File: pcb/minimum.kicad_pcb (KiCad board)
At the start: 4 copper layers, 16 x 20 mm, 31 parts, among them J1 USB4155-03-C_REVA, U1 RP2040, U2 SCD4x, U3 W25Q16JVUXIQ_WIN, U4 XCL220, Y1 C2E-12.000-18-1020-X-R

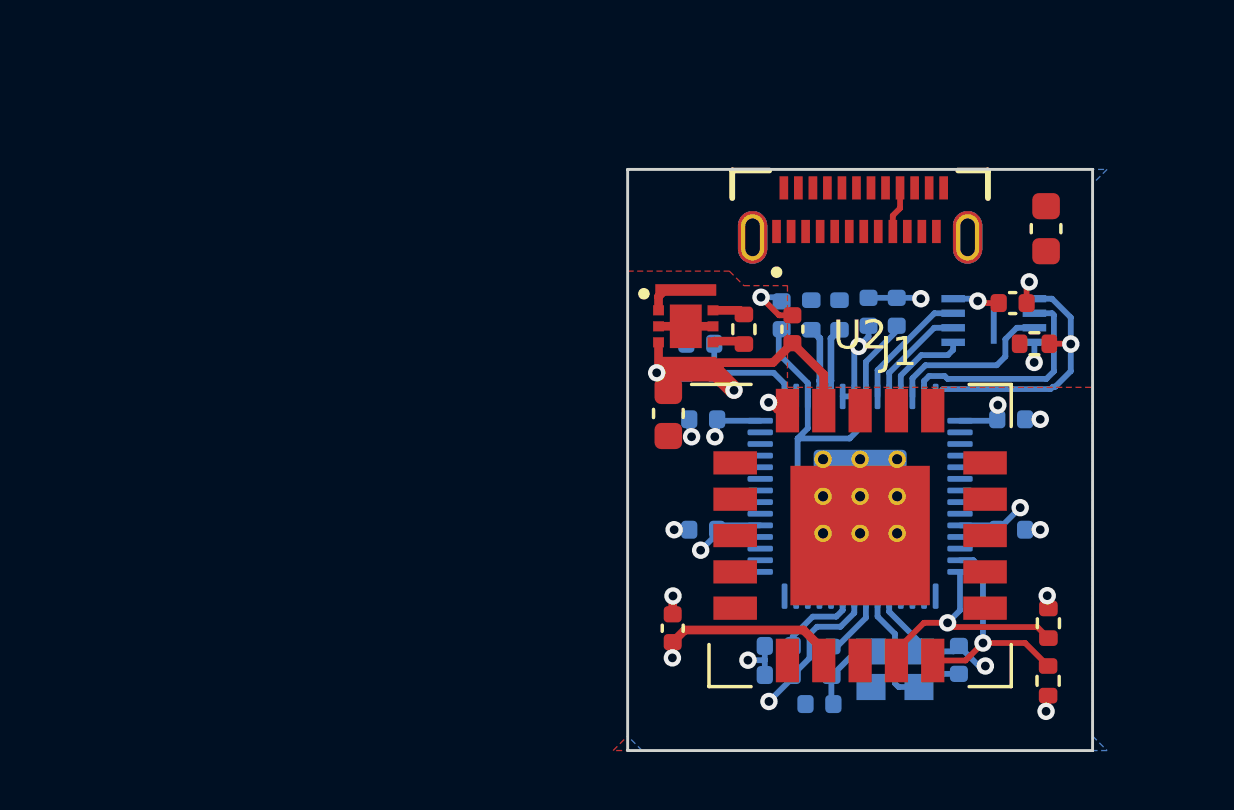
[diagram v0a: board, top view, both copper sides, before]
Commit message: USB plug connector changed to DX07P024MJ1R1500
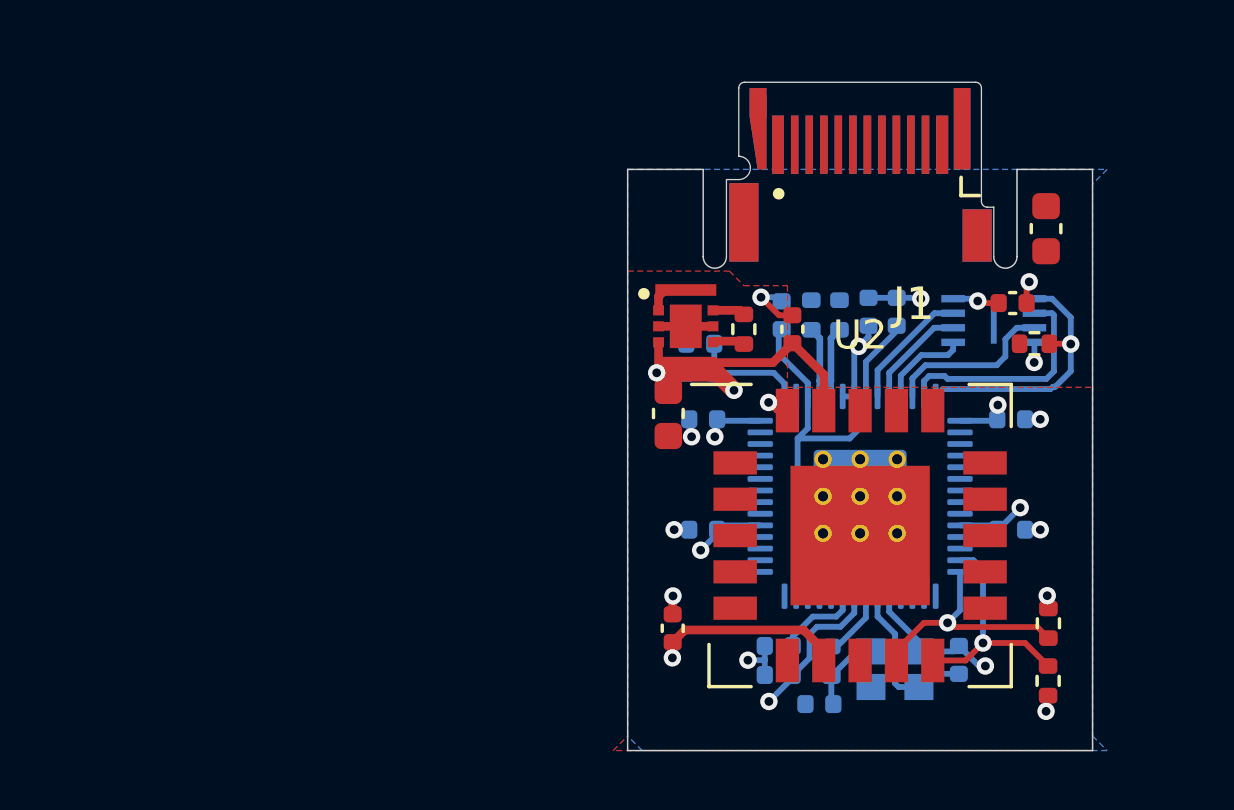
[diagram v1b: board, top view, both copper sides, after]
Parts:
- J1: value USB4155-03-C_REVA -> DX07P024MJ1R1500; footprint SMD:GCT_USB4155-03-C_REVA -> SMD:JAE_DX07P024MJ1R1500
- U3: value W25Q16JVUXIQ_WIN -> W25Q16JVUXIQ
- moved J1 4.39 mm to (100.0, 57.0)
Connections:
- J1 pad A10: (no net) -> unconnected-(J1-PadA10)
- J1 pad A11: (no net) -> unconnected-(J1-PadA11)
- J1 pad A2: (no net) -> unconnected-(J1-PadA2)
- J1 pad A3: (no net) -> unconnected-(J1-PadA3)
- J1 pad A4: VBUS -> Net-(J1-PadA4)
- J1 pad A5: (no net) -> unconnected-(J1-PadA5)
- J1 pad A6: /USB_D+ -> unconnected-(J1-PadA6)
- J1 pad A7: /USB_D- -> unconnected-(J1-PadA7)
- J1 pad A8: (no net) -> unconnected-(J1-PadA8)
- J1 pad A9: VBUS -> Net-(J1-PadA4)
- J1 pad B10: (no net) -> unconnected-(J1-PadB10)
- J1 pad B11: (no net) -> unconnected-(J1-PadB11)
- J1 pad B2: (no net) -> unconnected-(J1-PadB2)
- J1 pad B3: (no net) -> unconnected-(J1-PadB3)
- J1 pad B4: VBUS -> Net-(J1-PadB4)
- J1 pad B5: (no net) -> unconnected-(J1-PadB5)
- J1 pad B6: /USB_D+ -> unconnected-(J1-PadB6)
- J1 pad B7: /USB_D- -> unconnected-(J1-PadB7)
- J1 pad B8: (no net) -> unconnected-(J1-PadB8)
- J1 pad B9: VBUS -> Net-(J1-PadB4)
- J1 pad S1: Net-(J1-PadS1) -> (no net)
- J1 pad S2: Net-(J1-PadS1) -> (no net)
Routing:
- net VBUS: track 1.60 -> 0.00 mm
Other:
- outline, holes or cut-outs redrawn

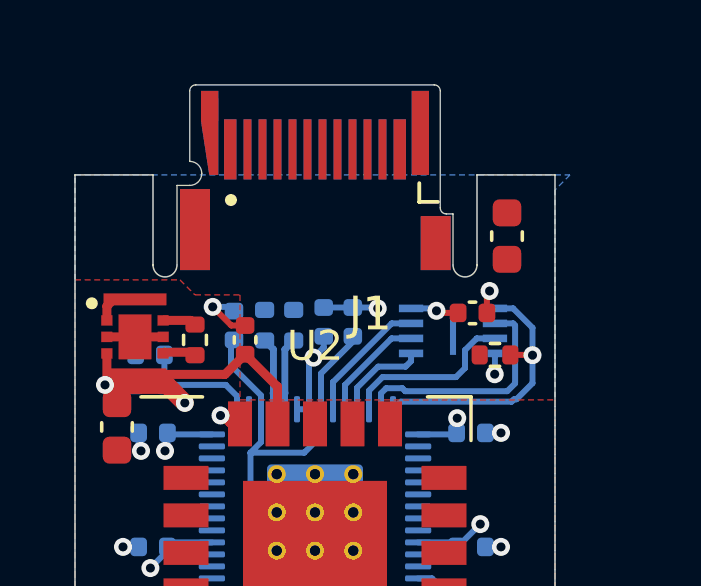
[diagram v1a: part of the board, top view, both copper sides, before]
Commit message: routing VBUS
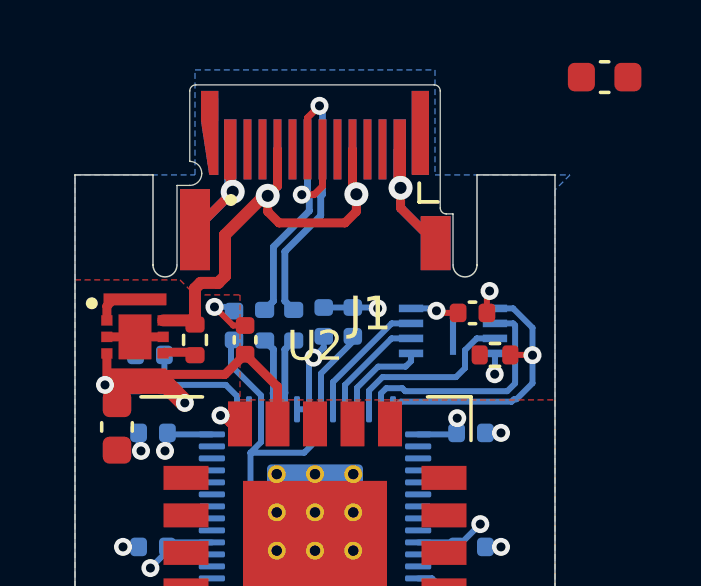
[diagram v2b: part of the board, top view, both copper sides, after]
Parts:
- moved C17 6.22 mm to (109.7, 56.7), turned to 180 degrees
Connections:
- J1 pad A1: Net-(J1-PadA1) -> GND
- J1 pad A10: unconnected-(J1-PadA10) -> (no net)
- J1 pad A11: unconnected-(J1-PadA11) -> (no net)
- J1 pad A12: Net-(J1-PadA1) -> GND
- J1 pad A2: unconnected-(J1-PadA2) -> (no net)
- J1 pad A3: unconnected-(J1-PadA3) -> (no net)
- J1 pad A4: Net-(J1-PadA4) -> VBUS
- J1 pad A5: unconnected-(J1-PadA5) -> (no net)
- J1 pad A6: unconnected-(J1-PadA6) -> /USB_D+
- J1 pad A7: unconnected-(J1-PadA7) -> /USB_D-
- J1 pad A8: unconnected-(J1-PadA8) -> (no net)
- J1 pad A9: Net-(J1-PadA4) -> VBUS
- J1 pad B1: Net-(J1-PadB1) -> GND
- J1 pad B10: unconnected-(J1-PadB10) -> (no net)
- J1 pad B11: unconnected-(J1-PadB11) -> (no net)
- J1 pad B12: Net-(J1-PadB1) -> GND
- J1 pad B2: unconnected-(J1-PadB2) -> (no net)
- J1 pad B3: unconnected-(J1-PadB3) -> (no net)
- J1 pad B4: Net-(J1-PadB4) -> VBUS
- J1 pad B5: unconnected-(J1-PadB5) -> (no net)
- J1 pad B6: unconnected-(J1-PadB6) -> /USB_D+
- J1 pad B7: unconnected-(J1-PadB7) -> /USB_D-
- J1 pad B8: unconnected-(J1-PadB8) -> (no net)
- J1 pad B9: Net-(J1-PadB4) -> VBUS
- J1 pad S3: Net-(J1-PadS3) -> GND
- J1 pad S4: Net-(J1-PadS3) -> GND
- J1 pad S5: Net-(J1-PadS3) -> GND
- J1 pad S6: Net-(J1-PadS3) -> GND
- R7 pad 1: +5V -> VBUS
- U4 pad 6: +5V -> VBUS
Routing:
- net VBUS: track 0.00 -> 17.7 mm, vias 0 -> 2
- net GND: track 19.4 -> 33.0 mm, vias 12 -> 14
- net /USB_D-: track 0.00 -> 9.62 mm, vias 0 -> 1
- net /USB_D+: track 0.00 -> 9.10 mm, vias 0 -> 1
- net +5V: track 1.12 -> 0.00 mm
- net +3V3: track 42.4 -> 43.4 mm

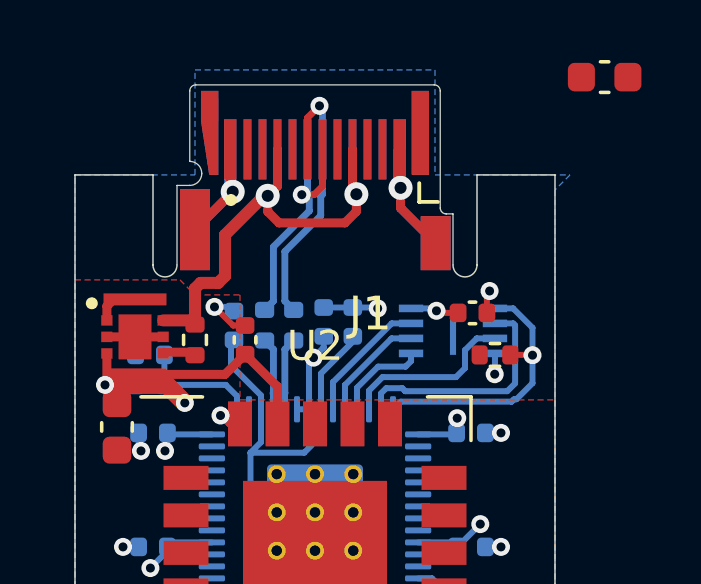
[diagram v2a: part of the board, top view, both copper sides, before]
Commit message: routing VBUS
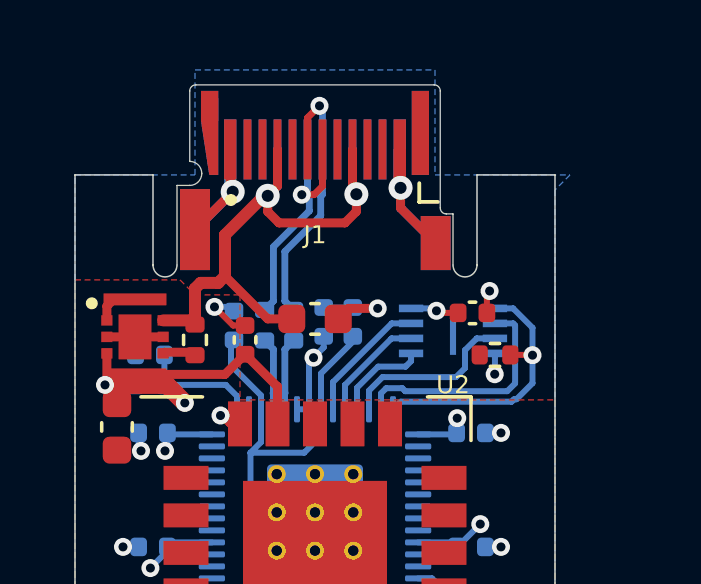
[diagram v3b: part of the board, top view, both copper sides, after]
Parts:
- moved C17 12.6 mm to (100.0, 64.8), turned to 0 degrees
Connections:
- C17 pad 1: (no net) -> VBUS
- C17 pad 2: (no net) -> GND
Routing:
- net VBUS: track 17.7 -> 20.5 mm
- net GND: track 33.0 -> 34.4 mm
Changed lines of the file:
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@@
     (property "Sheetname" "")
     (attr through_hole)
-    (fp_text reference "U2" (at 0 -6.9) (layer "F.SilkS")
-      (effects (font (size 1 1) (thickness 0.15)))
+    (fp_text reference "U2" (at 4.6 -5.6) (layer "F.SilkS")
+      (effects (font (size 0.6 0.6) (thickness 0.15)))
     )
     (fp_text value "SCD4x" (at 0 6.9) (layer "F.Fab")
@@
   )
   (footprint "Capacitor_SMD:C_0603_1608Metric" (layer "F.Cu")
-    (at 109.655 56.74 180)
+    (at 100 64.8)
     (descr "Capacitor SMD 0603 (1608 Metric), square (rectangular) end terminal, IPC_7351 nominal, (Body size source: IPC-SM-782 page 76, https://www.pcb-3d.com/wordpress/wp-content/uploads/ipc-sm-782a_amendment_1_and_2.pdf), generated with kicad-footprint-generator")
     (tags "capacitor")
@@
     (fp_line (start -0.8 0.4) (end -0.8 -0.4) (layer "F.Fab") (width 0.1))
     (fp_line (start 0.8 -0.4) (end 0.8 0.4) (layer "F.Fab") (width 0.1))
-    (pad "1" smd roundrect locked (at -0.775 0 180) (size 0.9 0.95) (layers "F.Cu" "F.Paste" "F.Mask") (roundrect_rratio 0.25)
-      (pintype "passive"))
-    (pad "2" smd roundrect locked (at 0.775 0 180) (size 0.9 0.95) (layers "F.Cu" "F.Paste" "F.Mask") (roundrect_rratio 0.25)
-      (pintype "passive"))
+    (pad "1" smd roundrect locked (at -0.775 0) (size 0.9 0.95) (layers "F.Cu" "F.Paste" "F.Mask") (roundrect_rratio 0.25)
+      (net 21 "VBUS") (pintype "passive"))
+    (pad "2" smd roundrect locked (at 0.775 0) (size 0.9 0.95) (layers "F.Cu" "F.Paste" "F.Mask") (roundrect_rratio 0.25)
+      (net 3 "GND") (pintype "passive"))
     (model "${KISYS3DMOD}/Capacitor_SMD.3dshapes/C_0603_1608Metric.wrl"
       (offset (xyz 0 0 0))
@@
     (property "Sheetname" "")
     (attr through_hole)
-    (fp_text reference "J1" (at -1.83903 -7.62843 180) (layer "F.SilkS")
-      (effects (font (size 1.125087 1.125087) (thickness 0.15)))
+    (fp_text reference "J1" (at 0 -5 180) (layer "F.SilkS")
+      (effects (font (size 0.6 0.6) (thickness 0.15)))
     )
     (fp_text value "DX07P024MJ1R1500" (at 9.24037 2.245715 180) (layer "F.Fab")
@@
   (segment (start 105.73 64.6) (end 105.73 63.96) (width 0.2) (layer "F.Cu") (net 3))
   (segment (start 97.2695 65.02) (end 96.6495 64.4) (width 0.2) (layer "F.Cu") (net 3))
+  (segment (start 101.125 64.45) (end 100.775 64.8) (width 0.3) (layer "F.Cu") (net 3))
   (segment (start 97.67 65.02) (end 97.2695 65.02) (width 0.2) (layer "F.Cu") (net 3))
   (segment (start 97.175 59.15) (end 97.175 60.480534) (width 0.3) (layer "F.Cu") (net 3))
@@
   (segment (start 105.73 63.96) (end 105.82 63.87) (width 0.2) (layer "F.Cu") (net 3))
   (segment (start 94.375 65.4) (end 94 65.025) (width 0.3) (layer "F.Cu") (net 3))
+  (segment (start 102.09 64.45) (end 101.125 64.45) (width 0.3) (layer "F.Cu") (net 3))
   (segment (start 102.825 60.403878) (end 102.852183 60.431061) (width 0.4) (layer "F.Cu") (net 3))
   (segment (start 102.852183 61.102183) (end 104.025 62.275) (width 0.3) (layer "F.Cu") (net 3))
@@
   (segment (start 101.378654 61.221346) (end 101 61.6) (width 0.3) (layer "F.Cu") (net 21))
   (segment (start 97 62) (end 97 63.374022) (width 0.4) (layer "F.Cu") (net 21))
+  (segment (start 98.425978 64.8) (end 97 63.374022) (width 0.3) (layer "F.Cu") (net 21))
   (segment (start 96 63.7875) (end 96 64.99) (width 0.4) (layer "F.Cu") (net 21))
   (segment (start 98.42382 61.22382) (end 98.8 61.6) (width 0.3) (layer "F.Cu") (net 21))
@@
   (segment (start 97 63.374022) (end 96.774022 63.6) (width 0.4) (layer "F.Cu") (net 21))
   (segment (start 98.302248 60.697752) (end 97 62) (width 0.4) (layer "F.Cu") (net 21))
+  (segment (start 99.225 64.8) (end 98.425978 64.8) (width 0.3) (layer "F.Cu") (net 21))
   (segment (start 96.1875 63.6) (end 96 63.7875) (width 0.4) (layer "F.Cu") (net 21))
   (segment (start 101.25 59.15) (end 101.25 60.515009) (width 0.3) (layer "F.Cu") (net 21))
